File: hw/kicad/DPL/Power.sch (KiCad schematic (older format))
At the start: 9 parts, among them U2 AP7215-33YG-13

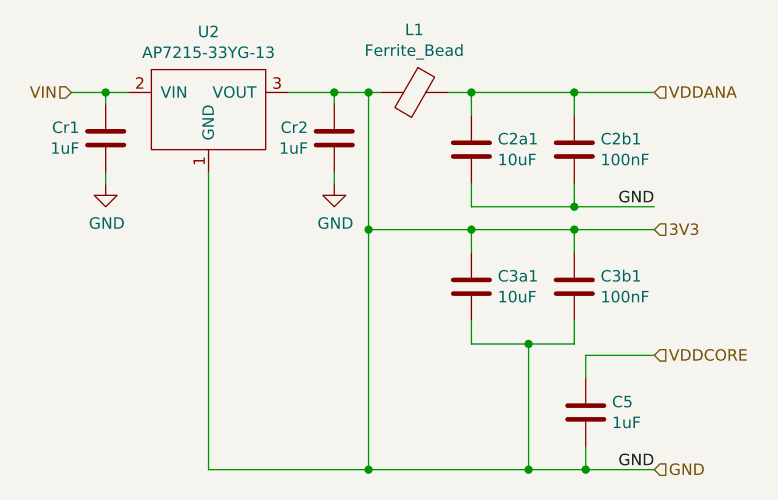
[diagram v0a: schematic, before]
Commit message: Changed the names of some components.
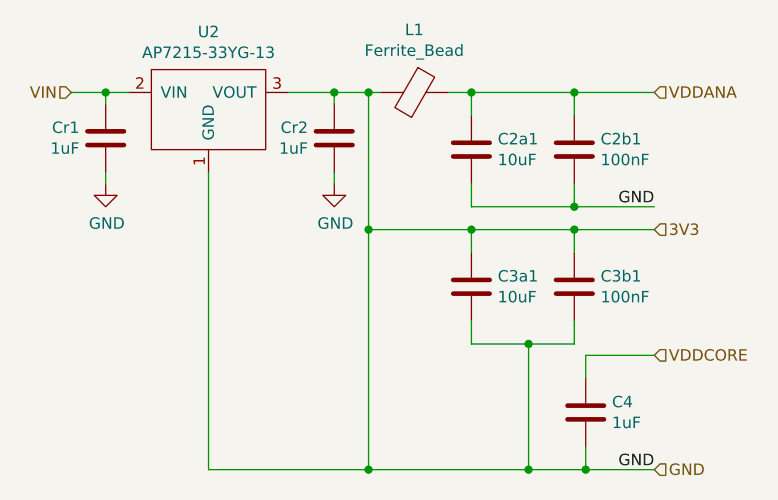
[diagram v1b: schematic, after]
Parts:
- renumbered C5 to C4
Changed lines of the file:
@@
 EESchema Schematic File Version 5
+LIBS:DPL-cache
 EELAYER 29 0
 EELAYER END
@@
 $EndComp
 $Comp
-L Device:C C5
+L Device:C C4
 U 1 1 5B635301
 P 5100 4800
-F 0 "C5" H 5215 4846 50  0000 L CNN
+F 0 "C4" H 5215 4846 50  0000 L CNN
 F 1 "1uF" H 5215 4755 50  0000 L CNN
 F 2 "Capacitor_SMD:C_0603_1608Metric_Pad1.05x0.95mm_HandSolder" H 5138 4650 50  0001 C CNN

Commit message: Added power selector to the board. Started to design the footprint's layout.
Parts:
- U2: footprint Package_TO_SOT_SMD:SOT-89-3_Handsoldering -> Package_TO_SOT_SMD:SOT-89-3
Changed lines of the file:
@@
 F 0 "U2" H 3450 3965 50  0000 C CNN
 F 1 "AP7215-33YG-13" H 3450 3874 50  0000 C CNN
-F 2 "Package_TO_SOT_SMD:SOT-89-3_Handsoldering" H 3450 3550 50  0001 C CNN
+F 2 "Package_TO_SOT_SMD:SOT-89-3" H 3450 3550 50  0001 C CNN
 F 3 "" H 3450 3550 50  0001 C CNN
 	1    3450 3550

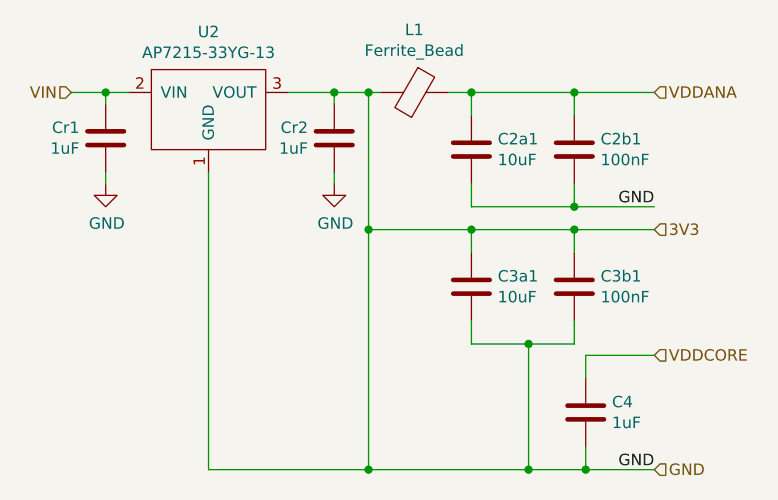
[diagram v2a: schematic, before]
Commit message: Fixed some conections errors. Designed the footprint. Added vias to pass the thread wire of the balloons through them.
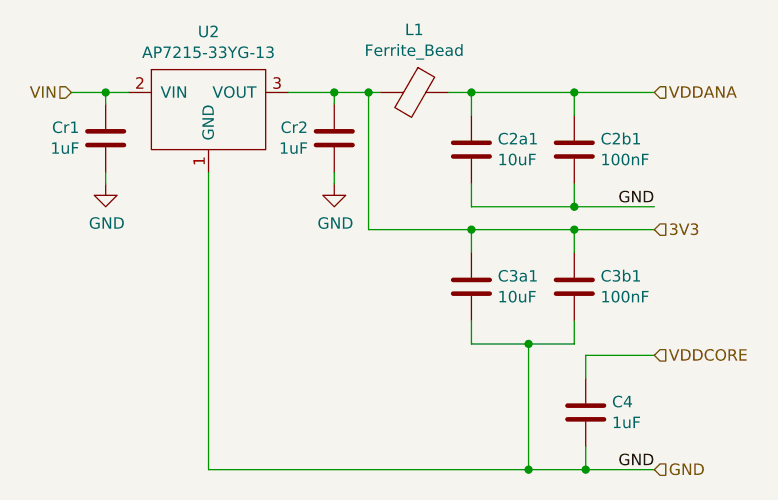
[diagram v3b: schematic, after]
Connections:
- net GND: no longer C3a1.1, C3b1.1, Cr2.1, L1.2, U2.3 (VOUT)
- new net 3V3: C3a1.1, C3b1.1, Cr2.1, L1.2, U2.3 (VOUT)
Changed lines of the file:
@@
 Text HLabel 5400 5050 2    50   Input ~ 0
 GND
-Wire Wire Line
-	4150 5050 4850 5050
 Connection ~ 5100 5050
 Text Label 5400 3900 2    50   ~ 0
@@
 Text Label 5400 5050 2    50   ~ 0
 GND
-Connection ~ 4150 4000
 Wire Wire Line
 	4150 4000 4150 3400
@@
 	5400 4000 5050 4000
 Connection ~ 5050 4000
-Connection ~ 4150 5050
 Text HLabel 2850 3400 0    50   Input ~ 0
 VIN
@@
 	3450 5050 3450 3750
 Wire Wire Line
-	3450 5050 4150 5050
-Wire Wire Line
-	4150 4000 4150 5050
+	3450 5050 4850 5050
 $EndSCHEMATC
